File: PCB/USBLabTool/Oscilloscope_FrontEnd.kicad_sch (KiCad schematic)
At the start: 92 parts, among them J10 T_pwm, J12 T_buf, J14 ADC1, J15 ADC2, J16 +3.3VA, J4 T_att, J5 T_acdc, J6 T_acdc, J8 T_amp, J9 T_amp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

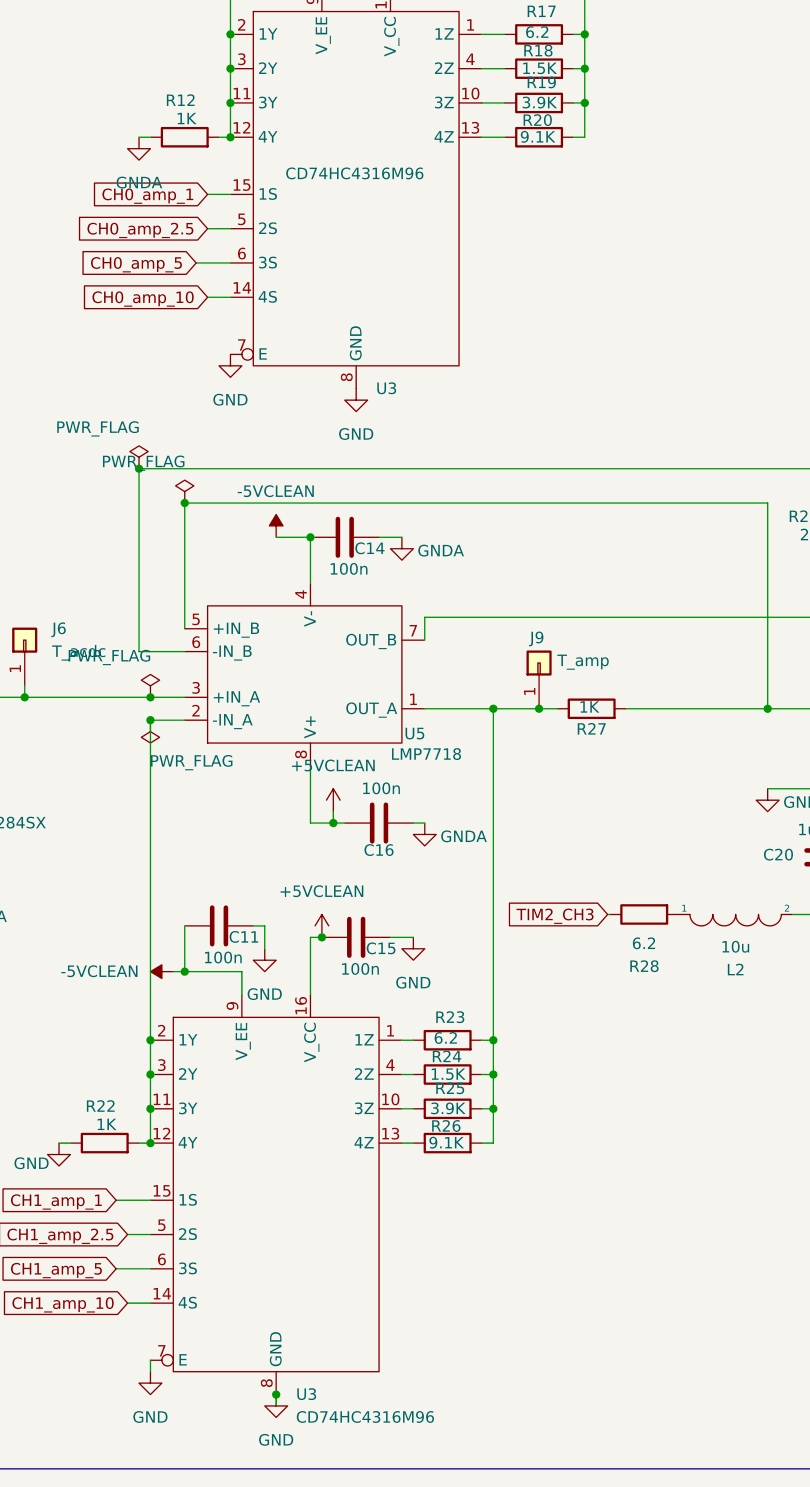
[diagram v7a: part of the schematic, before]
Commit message: update switch name
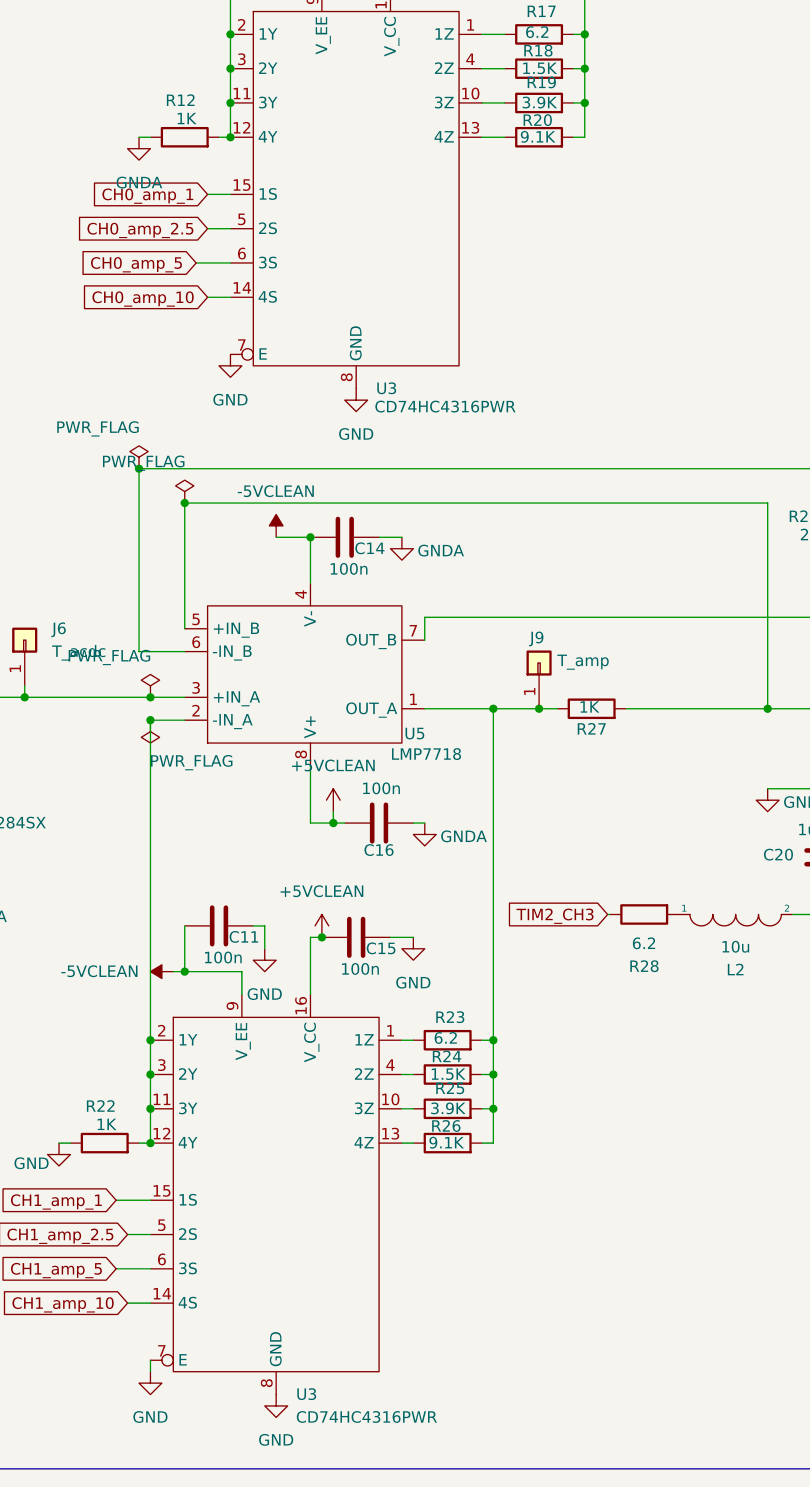
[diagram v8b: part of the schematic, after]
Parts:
- U3: value CD74HC4316M96 -> CD74HC4316PWR
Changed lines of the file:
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@@
 	)
 	(junction
-		(at 162.56 241.3)
-		(diameter 0)
-		(color 0 0 0 0)
-	)
-	(junction
 		(at 157.48 101.6)
 		(diameter 0)
@@
 	(wire
 		(pts
-			(xy 162.56 242.57) (xy 162.56 241.3)
-		)
-		(stroke
-			(width 0)
-			(type default)
-		)
-	)
-	(wire
-		(pts
 			(xy 288.29 181.61) (xy 287.02 181.61)
 		)
@@
 	)
 	(symbol
-		(lib_name "GND_5")
-		(lib_id "power:GND")
-		(at 162.56 241.3 0)
-		(unit 1)
-		(exclude_from_sim no)
-		(in_bom yes)
-		(on_board yes)
-		(dnp no)
-		(fields_autoplaced yes)
-		(property "Reference" "#PWR018"
-			(at 162.56 247.65 0)
-			(effects
-				(font
-					(size 1.27 1.27)
-				)
-				(hide yes)
-			)
-		)
-		(property "Value" "GND"
-			(at 162.56 246.38 0)
-			(effects
-				(font
-					(size 1.27 1.27)
-				)
-			)
-		)
-		(property "Footprint" ""
-			(at 162.56 241.3 0)
-			(effects
-				(font
-					(size 1.27 1.27)
-				)
-				(hide yes)
-			)
-		)
-		(property "Datasheet" ""
-			(at 162.56 241.3 0)
-			(effects
-				(font
-					(size 1.27 1.27)
-				)
-				(hide yes)
-			)
-		)
-		(property "Description" ""
-			(at 162.56 241.3 0)
-			(effects
-				(font
-					(size 1.27 1.27)
-				)
-				(hide yes)
-			)
-		)
-		(pin "1"
-		)
-		(instances
-			(project "USBLabTool"
-				(path "/b5440f7d-90d5-417e-adc2-aa6b11e5424d/4269701b-4537-45be-98a2-a1633b405066"
-					(reference "#PWR018")
-					(unit 1)
-				)
-			)
-		)
-	)
-	(symbol
 		(lib_name "-5V_4")
 		(lib_id "power:-5V")
@@
 			)
 		)
-		(property "Value" "CD74HC4316M96"
+		(property "Value" "CD74HC4316PWR"
 			(at 164.7541 243.84 0)
 			(effects
@@
 			)
 		)
-		(property "Datasheet" "https://www.digikey.com/en/products/detail/texas-instruments/CD74HC4316M96/555784"
+		(property "Datasheet" "https://www.digikey.com/en/products/detail/texas-instruments/CD74HC4316PWR/1507290"
 			(at 149.86 198.12 0)
 			(effects
@@
 			)
 		)
-		(property "Value" "CD74HC4316M96"
-			(at 163.576 105.664 0)
+		(property "Value" "CD74HC4316PWR"
+			(at 173.482 131.572 0)
 			(effects
 				(font
@@
 			)
 		)
-		(property "Datasheet" "https://www.digikey.com/en/products/detail/texas-instruments/CD74HC4316M96/555784"
+		(property "Datasheet" "https://www.digikey.com/en/products/detail/texas-instruments/CD74HC4316PWR/1507290"
 			(at 158.75 86.36 0)
 			(effects
@@
 					(unit 1)
 				)
+			)
+		)
+	)
+	(symbol
+		(lib_name "GND_5")
+		(lib_id "power:GND")
+		(at 162.56 241.3 0)
+		(unit 1)
+		(exclude_from_sim no)
+		(in_bom yes)
+		(on_board yes)
+		(dnp no)
+		(fields_autoplaced yes)
+		(property "Reference" "#PWR018"
+			(at 162.56 247.65 0)
+			(effects
+				(font
+					(size 1.27 1.27)
+				)
+				(hide yes)
+			)
+		)
+		(property "Value" "GND"
+			(at 162.56 246.38 0)
+			(effects
+				(font
+					(size 1.27 1.27)
+				)
+			)
+		)
+		(property "Footprint" ""
+			(at 162.56 241.3 0)
+			(effects
+				(font
+					(size 1.27 1.27)
+				)
+				(hide yes)
+			)
+		)
+		(property "Datasheet" ""
+			(at 162.56 241.3 0)
+			(effects
+				(font
+					(size 1.27 1.27)
+				)
+				(hide yes)
+			)
+		)
+		(property "Description" "Power symbol creates a global label with name \"GND\" , ground"
+			(at 162.56 241.3 0)
+			(effects
+				(font
+					(size 1.27 1.27)
+				)
+				(hide yes)
+			)
+		)
+		(pin "1"
+		)
+		(instances
+			(project ""
+				(path "/b5440f7d-90d5-417e-adc2-aa6b11e5424d/4269701b-4537-45be-98a2-a1633b405066"
+					(reference "#PWR018")
+					(unit 1)
+				)
